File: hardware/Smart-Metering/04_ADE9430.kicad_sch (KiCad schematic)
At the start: 0 parts

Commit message: Inicia núcleo metrológico com ADE9430
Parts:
- added U1: ADE9430ACPZ, symbol SmartMetering:ADE9430
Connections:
- new net +3V3_ADE: U1.40 (SS)
- new net CF1_ADE: U1.34 (CF2)
- new net CF2_ADE: U1.33 (CF1)
- new net DREADY_ADE: U1.31 (IRQ0)
- new net GND: U1.39 (MOSI)
- new net IRQ0_ADE: U1.36 (CF4/EVENT/DREADY)
- new net IRQ1_ADE: U1.35 (CF3/ZX)
- new net MISO_ADE: U1.29 (CLKIN)
- new net MOSI_ADE: U1.28 (GND)
- new net SCLK_ADE: U1.30 (CLKOUT)
- new net SS_ADE: U1.27 (VDD)
- new net XIN_ADE: U1.38 (MISO)
- new net XOUT_ADE: U1.37 (SCLK)
- new net ZX_ADE: U1.32 (IRQ1)
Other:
- note added: "ADE9430 metrology core 40-lead LFCSP, 6 x 6 mm, EPAD All analog channels are differential. PM0 and PM1 are tied to GND for normal operation. PULL_HIGH and VDD use +3V3_ADE."
- company: (none) -> Smart-Metering
- title: (none) -> ADE9430 - Metrology Core

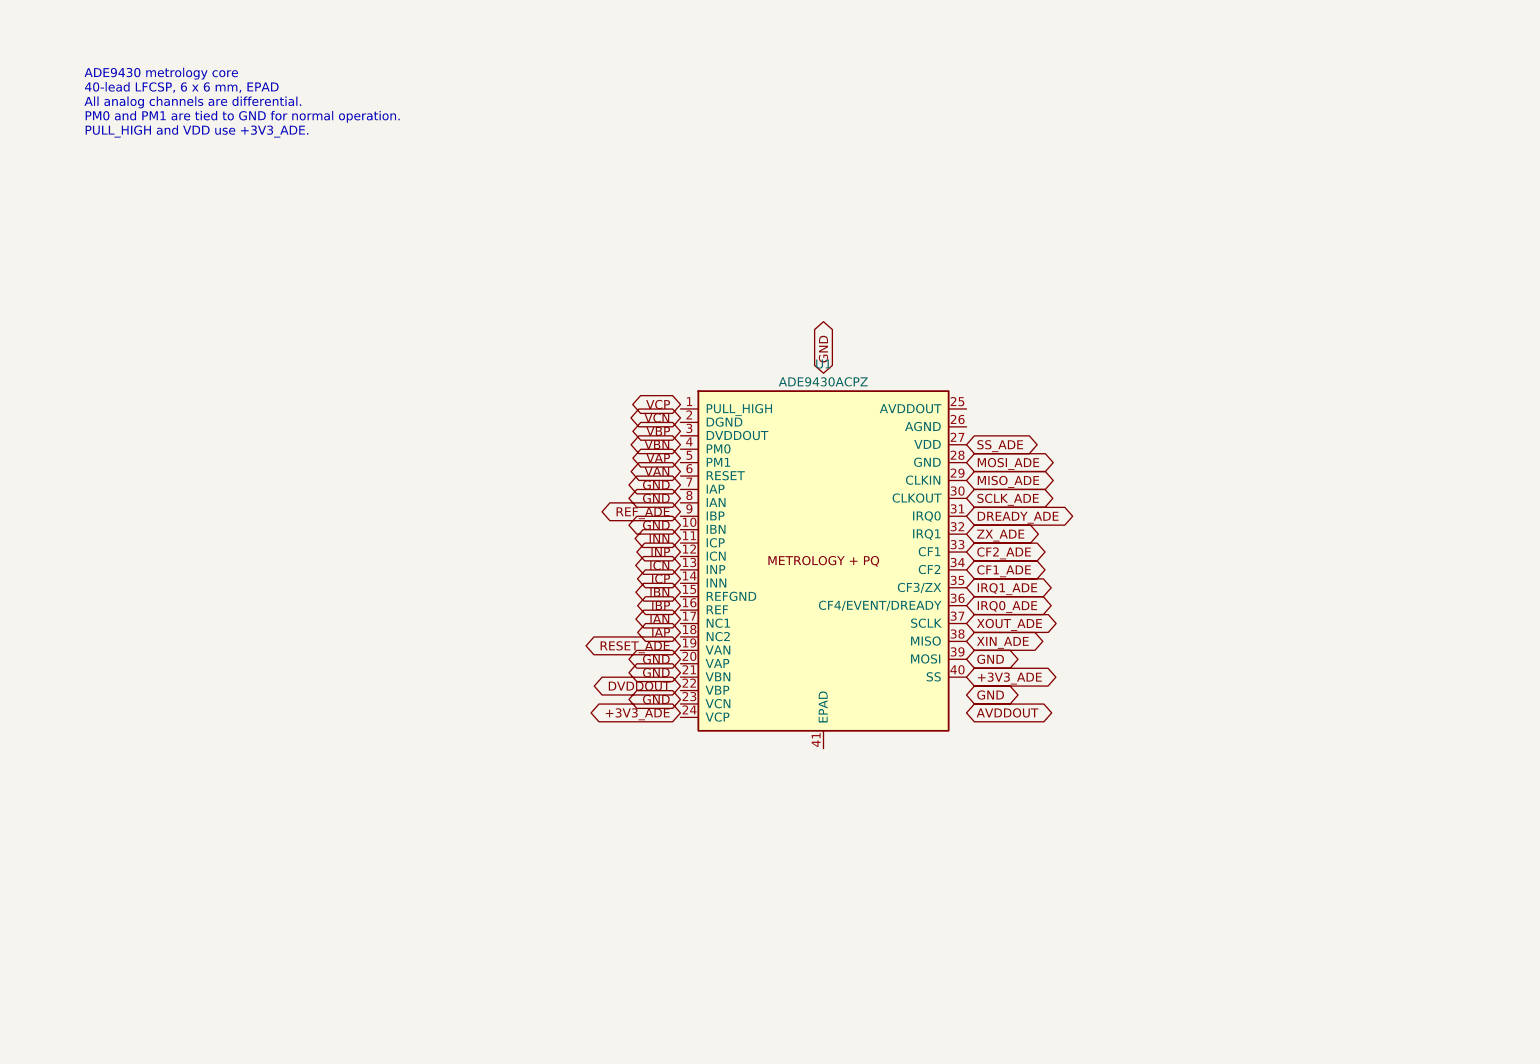
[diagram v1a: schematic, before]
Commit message: Completa alimentação, clock e reset do ADE9430
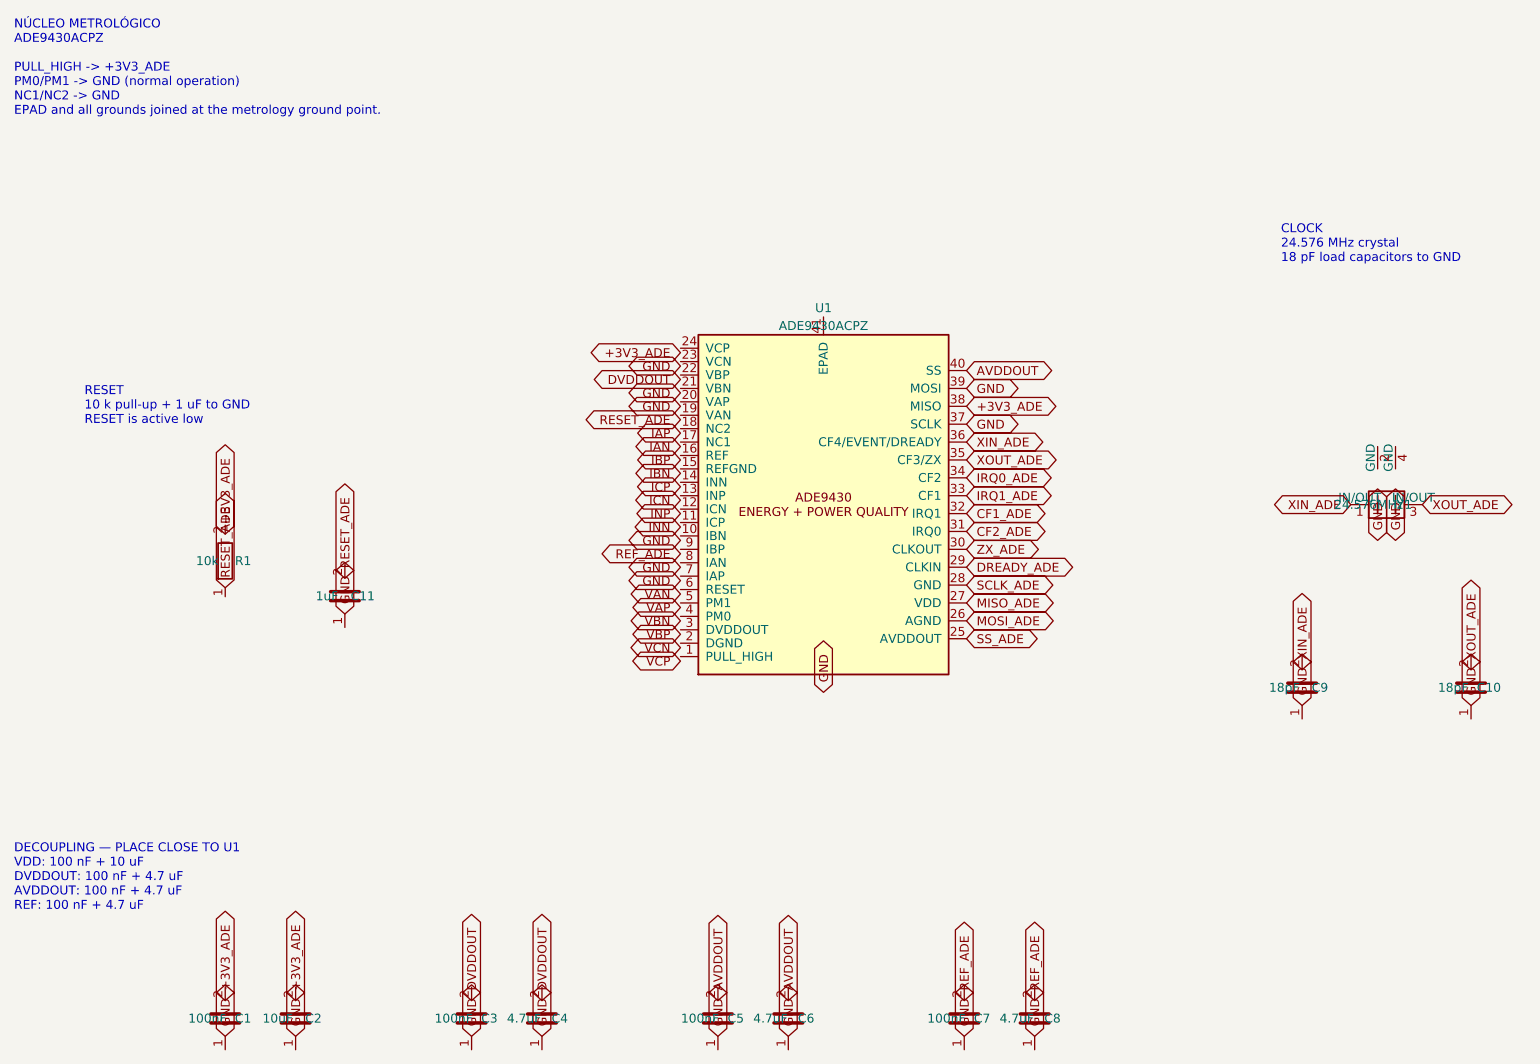
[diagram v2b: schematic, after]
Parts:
- added C1, C3, C5, C7: 100nF, Capacitor_SMD:C_0603_1608Metric, symbol SmartMetering:C_Vert
- added C10, C9: 18pF, Capacitor_SMD:C_0603_1608Metric, symbol SmartMetering:C_Vert
- added C11: 1uF, Capacitor_SMD:C_0603_1608Metric, symbol SmartMetering:C_Vert
- added C2: 10uF, Capacitor_SMD:C_0805_2012Metric, symbol SmartMetering:C_Vert
- added C4, C6, C8: 4.7uF, Capacitor_SMD:C_0805_2012Metric, symbol SmartMetering:C_Vert
- added R1: 10k, Resistor_SMD:R_0603_1608Metric, symbol SmartMetering:R_Vert
- added Y1: 24.576MHz, Crystal:Crystal_SMD_3225-4Pin_3.2x2.5mm, symbol SmartMetering:Crystal_4Pin
- U1: footprint (none) -> Package_DFN_QFN:LFCSP-40-1EP_6x6mm_P0.5mm_EP4.5x4.5mm
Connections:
- net +3V3_ADE: now also U1.38 (MISO), C1.2, C2.2, R1.2; no longer U1.40 (SS)
- net AVDDOUT: now also U1.40 (SS), C5.2, C6.2
- net CF1_ADE: now also U1.32 (IRQ1); no longer U1.34 (CF2)
- net CF2_ADE: now also U1.31 (IRQ0); no longer U1.33 (CF1)
- net DREADY_ADE: now also U1.29 (CLKIN); no longer U1.31 (IRQ0)
- net DVDDOUT: now also C3.2, C4.2
- net GND: now also U1.37 (SCLK), C1.1, C10.1, C11.1, C2.1, C3.1, C4.1, C5.1, C6.1, C7.1, C8.1, C9.1
- net IRQ0_ADE: now also U1.34 (CF2); no longer U1.36 (CF4/EVENT/DREADY)
- net IRQ1_ADE: now also U1.33 (CF1); no longer U1.35 (CF3/ZX)
- net MISO_ADE: now also U1.27 (VDD); no longer U1.29 (CLKIN)
- net MOSI_ADE: now also U1.26 (AGND); no longer U1.28 (GND)
- net REF_ADE: now also C7.2, C8.2
- net RESET_ADE: now also C11.2, R1.1
- net SCLK_ADE: now also U1.28 (GND); no longer U1.30 (CLKOUT)
- net SS_ADE: now also U1.25 (AVDDOUT); no longer U1.27 (VDD)
- net XIN_ADE: now also U1.36 (CF4/EVENT/DREADY), C9.2, Y1.1 (IN/OUT); no longer U1.38 (MISO)
- net XOUT_ADE: now also U1.35 (CF3/ZX), C10.2, Y1.3 (IN/OUT); no longer U1.37 (SCLK)
- net ZX_ADE: now also U1.30 (CLKOUT); no longer U1.32 (IRQ1)
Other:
- note added: "CLOCK 24.576 MHz crystal 18 pF load capacitors to GND"
- note added: "DECOUPLING — PLACE CLOSE TO U1 VDD: 100 nF + 10 uF DVDDOUT: 100 nF + 4.7 uF AVDDOUT: 100 nF + 4.7 uF REF: 100 nF + 4.7 uF"
- note added: "NÚCLEO METROLÓGICO ADE9430ACPZ PULL_HIGH -> +3V3_ADE PM0/PM1 -> GND (normal operation) NC1/NC2 -> GND EPAD and all grounds joined at the metrology ground point."
- note added: "RESET 10 k pull-up + 1 uF to GND RESET is active low"
- note removed: "ADE9430 metrology core 40-lead LFCSP, 6 x 6 mm, EPAD All analog channels are differential. PM0 and PM1 are tied to GND for normal operation. PULL_HIGH and VDD use +3V3_ADE."
